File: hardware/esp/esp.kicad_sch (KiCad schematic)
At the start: 0 parts

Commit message: Updating PCB
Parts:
- added J1: USB_C_Receptacle_USB2.0_16P, Connector_USB:USB_C_Receptacle_HCTL_HC-TYPE-C-16P-01A, symbol Connector:USB_C_Receptacle_USB2.0_16P
- added J2: Conn_01x02, symbol Connector_Generic:Conn_01x02
- added L1: L, symbol Device:L
- added R1, R2: 22R, symbol Device:R
- added U1: BME280, Package_LGA:Bosch_LGA-8_2.5x2.5mm_P0.65mm_ClockwisePinNumbering, symbol Sensor:BME280
- added U2: VL53L0X, VL53L0X:SENSOR_VL53L0X, symbol VL53L0X:VL53L0X
- added U3: NRF24L01, Package_DFN_QFN:QFN-20-1EP_4x4mm_P0.5mm_EP2.5x2.5mm, symbol RF:NRF24L01
- added U4: ESP32-S3-WROOM-1, RF_Module:ESP32-S3-WROOM-1, symbol RF_Module:ESP32-S3-WROOM-1
- added U5: NT3H1101W0FHK, NT3H1101W0FHK:IC_NT3H1101W0FHK, symbol NT3H1101W0FHK:NT3H1101W0FHK
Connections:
- new net: U4.1 (GND), U4.40 (GND), U4.41 (GND)
- new net: L1.1, U5.8 (LB)
- new net: L1.2, U5.1 (LA)
- new net: J1.A6 (D+), J1.B6 (D+), R2.1
- new net: J1.A7 (D-), J1.B7 (D-), R1.1
- new net +5V: J1.A4 (VBUS), J1.A9 (VBUS), J1.B4 (VBUS), J1.B9 (VBUS)
- new net D+: R2.2, U4.14 (USB_D+)
- new net D-: R1.2, U4.13 (USB_D-)
- new net GND: J1.A1 (GND), J1.A12 (GND), J1.B1 (GND), J1.B12 (GND), J1.SH (SHIELD), U2.12 (GND), U2.3 (GND), U2.4 (GND), U2.6 (GND)
- new net UART_SRX: J2.2 (Pin_2)
- new net UART_STX: J2.1 (Pin_1)

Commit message: Updating schematics
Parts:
- removed U3: NRF24L01, Package_DFN_QFN:QFN-20-1EP_4x4mm_P0.5mm_EP2.5x2.5mm, symbol RF:NRF24L01
- added C1: 10nF, Capacitor_SMD:C_0603_1608Metric, symbol Device:C
- added C10, C11: C, symbol Device:C
- added C12: 100nF, symbol Device:C
- added C13: 4.7pF, symbol Device:C
- added C2: 33nF, Capacitor_SMD:C_0603_1608Metric, symbol Device:C
- added C3: 1nF, Capacitor_SMD:C_0603_1608Metric, symbol Device:C
- added C4: 2.2pF, Capacitor_SMD:C_0603_1608Metric, symbol Device:C
- added C5, C6: 22pF, Capacitor_SMD:C_0603_1608Metric, symbol Device:C
- added C7: 4.7pF, Capacitor_SMD:C_0603_1608Metric, symbol Device:C
- added C8: 1.5pF, Capacitor_SMD:C_0603_1608Metric, symbol Device:C
- added C9: 1pF, Capacitor_SMD:C_0603_1608Metric, symbol Device:C
- added L2: 8.2nH, Inductor_SMD:L_0603_1608Metric, symbol Device:L
- added L3, L4: 2.7nH, Inductor_SMD:L_0603_1608Metric, symbol Device:L
- added R1: 22K, Resistor_SMD:R_0603_1608Metric, symbol Device:R
- added R10, R11, R12: R, symbol Device:R
- added R13, R7, R8, R9: 1.5K, symbol Device:R
- added R4, R5: 5.1k, symbol Device:R
- added R6: 1M, Resistor_SMD:R_0603_1608Metric, symbol Device:R
- added U2: NRF24L01, Package_DFN_QFN:QFN-20-1EP_4x4mm_P0.5mm_EP2.5x2.5mm, symbol RF:NRF24L01
- added Y1: 16MHz, Crystal:Crystal_SMD_3225-4Pin_3.2x2.5mm, symbol Device:Crystal_GND24
- renumbered J2 to J3, R1 to R2, R2 to R3, U5 to U1, U4 to U3, U2 to U4, U1 to U5
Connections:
- net GND: now also U1.2 (VSS), U3.1 (GND), U3.40 (GND), U3.41 (GND), U4.2 (AVSSVCSEL), U5.1 (GND), U5.7 (GND), C1.1, C10.1, C11.2, C12.2, C13.2, C2.2, C3.1, C4.2, C5.1, C6.2, C7.2, C9.1, R1.1, R4.2, R5.2, U2.14 (VSS), U2.17 (VSS), U2.20 (VSS), U2.8 (VSS), Y1.2 (G), Y1.4 (G)
- net SDA: now reaches U3.12 (IO8)
- net SDA: now also U1.5 (SDA), U4.9 (SDA), U5.3 (SDI), R10.2, R7.2
- net SCL: now reaches U3.17 (IO9)
- net SCL: now also U1.3 (SCL), U4.10 (SCL), U5.4 (SCK), R11.1, R8.2
- net NFC_FD: now reaches U1.4 (FD)
- net +3V3: now reaches U1.6 (VCC)
- net +3V3: now also U4.1 (AVDDVCSEL), U4.11 (AVDD), U5.6 (VDDIO), U5.8 (VDD), C1.2, C10.2, C11.1, C12.1, C13.1, C3.2, R10.1, R11.2, R12.1, R13.1, R7.1, R8.1, R9.1, U2.15 (VDD), U2.18 (VDD), U2.7 (VDD)
- net XSHUT: now reaches U4.5 (~{XSHUT})
- net XSHUT: now also R9.2
- net DIST_GPIO1: now reaches U4.7 (GPIO1)
- net DIST_GPIO1: now also R13.2
- net at U5.2 (CSB): now also R12.2
- net at J1.A5 (CC1): now also R4.1
- net at J1.B5 (CC2): now also R5.1
- new net: C8.1, L3.2
- new net: C8.2, C9.2
- new net: L2.1, L3.1, U2.13 (ANT2)
- new net: C4.1, C7.1, L4.2, U2.11 (VDD_PA)
- new net: C5.2, R6.1, U2.10 (XC1), Y1.3
- new net: C6.1, R6.2, U2.9 (XC2), Y1.1
- new net: L2.2, L4.1, U2.12 (ANT1)
- new net: R1.2, U2.16 (IREF)
- new net: C2.1, U2.19 (DVDD)
- new net NRF_CE: U2.1 (CE)
- new net NRF_CSN: U2.2 (CSN)
- new net SPI_MISO: U2.5 (MISO)
- new net SPI_MOSI: U2.4 (MOSI)
- new net SPI_SCK: U2.3 (SCK)
- no-connect marks 0 -> 8
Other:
- note added: "ANT"
- note added: "NRF24l01"
- moved on the sheet: J3, L1, U1, U3, U4, U5

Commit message: Updating PCb and esp board schematics
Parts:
- added C10, C6: C, symbol Device:C
- added C12: 0.1µF, Capacitor_SMD:C_0805_2012Metric, symbol Device:C
- added D1, D2, D3, D4, D5, D6, D7: LED, symbol Device:LED
- added R1, R11, R12, R13, R14, R15, R2: R, symbol Device:R
- added R10: 10K, Resistor_SMD:R_0805_2012Metric, symbol Device:R
- added R9: 10k, Resistor_SMD:R_0805_2012Metric, symbol Device:R
- added SW1: RESET, Button_Switch_SMD:SW_SPST_SKQG_WithStem, symbol Switch:SW_Push
- added SW2: BOOT, Button_Switch_SMD:SW_SPST_SKQG_WithStem, symbol Switch:SW_Push
- C13: renamed from C10; footprint (none) -> Capacitor_SMD:C_0603_1608Metric
- C14: renamed from C12; footprint (none) -> Capacitor_SMD:C_0603_1608Metric
- C15: renamed from C11; footprint (none) -> Capacitor_SMD:C_0603_1608Metric
- C16: renamed from C13; footprint (none) -> Capacitor_SMD:C_0603_1608Metric
- R16: renamed from R7; footprint (none) -> Resistor_SMD:R_0805_2012Metric
- R17: renamed from R8; footprint (none) -> Resistor_SMD:R_0805_2012Metric
- R18: renamed from R9; footprint (none) -> Resistor_SMD:R_0805_2012Metric
- R19: renamed from R10; footprint (none) -> Resistor_SMD:R_0805_2012Metric
- R20: renamed from R13; footprint (none) -> Resistor_SMD:R_0805_2012Metric
- R21: renamed from R11; footprint (none) -> Resistor_SMD:R_0805_2012Metric
- R22: renamed from R12; footprint (none) -> Resistor_SMD:R_0805_2012Metric
- R4: renamed from R2; footprint (none) -> Resistor_SMD:R_0805_2012Metric
- R5: renamed from R3; footprint (none) -> Resistor_SMD:R_0805_2012Metric
- R6: renamed from R4; footprint (none) -> Resistor_SMD:R_0805_2012Metric
- R7: renamed from R5; footprint (none) -> Resistor_SMD:R_0805_2012Metric
- R8: renamed from R6; footprint Resistor_SMD:R_0603_1608Metric -> Resistor_SMD:R_0805_2012Metric
- renumbered C9 to C11, C3 to C2, C2 to C3, C5 to C4, C4 to C5, C6 to C7, C7 to C8, C8 to C9, J3 to J2, R1 to R3
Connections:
- net +3V3: now also U3.2 (3V3), C10.2, C6.2, R10.1, R9.2
- net GND: now also C10.1, C12.1, C6.1, D1.1 (K), D2.1 (K), D5.1 (K), D6.1 (K), D7.1 (K), SW1.2, SW2.2; no longer U2.20 (VSS)
- net C.SKULL: now reaches U3.15 (IO3)
- net C.SKULL: now also R14.1
- net BOOT: now reaches U3.27 (IO0)
- net BOOT: now also R10.2, SW2.1
- net EN: now reaches U3.3 (EN)
- net EN: now also C12.2, R9.1, SW1.1
- net O.SKULL: now reaches U3.38 (IO2)
- net O.SKULL: now also R13.1
- net NRFLED: now reaches U3.39 (IO1)
- net NRFLED: now also R2.1
- net NF.SKULL: now reaches U3.4 (IO4)
- net NF.SKULL: now also R15.1
- net NFCLED: now reaches U3.5 (IO5)
- net NFCLED: now also R1.1
- new net: D7.2 (A), R15.2
- new net: D2.2 (A), R2.2
- new net: D3.2 (A), R11.2
- new net: D5.2 (A), R13.2
- new net: D1.2 (A), R1.2
- new net: D4.2 (A), R12.2
- new net: D6.2 (A), R14.2
- no-connect marks 8 -> 10
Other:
- note added: "MCU"
- note added: "NFC chip"
- note added: "Skull opening detector"
- note added: "Temperature sensor"
- moved on the sheet: C1, C14, C16, C2, C4, J2, L1, R16, R17, R18, R20, U1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

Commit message: Updating schematics and PCB
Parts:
- removed C11: 1pF, Capacitor_SMD:C_0603_1608Metric, symbol Device:C
- removed C13, C15: C, Capacitor_SMD:C_0603_1608Metric, symbol Device:C
- removed C14: 100nF, Capacitor_SMD:C_0603_1608Metric, symbol Device:C
- removed C16, C8: 4.7pF, Capacitor_SMD:C_0603_1608Metric, symbol Device:C
- removed C5: 2.2pF, Capacitor_SMD:C_0603_1608Metric, symbol Device:C
- removed C7: 22pF, Capacitor_SMD:C_0603_1608Metric, symbol Device:C
- removed C9: 1.5pF, Capacitor_SMD:C_0603_1608Metric, symbol Device:C
- removed D2, D5, D6, D7: LED, symbol Device:LED
- removed L1: L, symbol Device:L
- removed L2: 8.2nH, Inductor_SMD:L_0603_1608Metric, symbol Device:L
- removed L3, L4: 2.7nH, Inductor_SMD:L_0603_1608Metric, symbol Device:L
- removed R1, R13, R14, R15, R2: R, symbol Device:R
- removed R16, R17, R18, R20: 1.5K, Resistor_SMD:R_0805_2012Metric, symbol Device:R
- removed R19, R21, R22: R, Resistor_SMD:R_0805_2012Metric, symbol Device:R
- removed R3: 22K, Resistor_SMD:R_0603_1608Metric, symbol Device:R
- removed R8: 1M, Resistor_SMD:R_0805_2012Metric, symbol Device:R
- removed U1: NT3H1101W0FHK, NT3H1101W0FHK:IC_NT3H1101W0FHK, symbol NT3H1101W0FHK:NT3H1101W0FHK
- removed U2: NRF24L01, Package_DFN_QFN:QFN-20-1EP_4x4mm_P0.5mm_EP2.5x2.5mm, symbol RF:NRF24L01
- removed U4: VL53L0X, VL53L0X:SENSOR_VL53L0X, symbol VL53L0X:VL53L0X
- removed U5: BME280, Package_LGA:Bosch_LGA-8_2.5x2.5mm_P0.65mm_ClockwisePinNumbering, symbol Sensor:BME280
- removed Y1: 16MHz, Crystal:Crystal_SMD_3225-4Pin_3.2x2.5mm, symbol Device:Crystal_GND24
- added J3: USB_C_Receptacle_USB2.0_16P, Connector_USB:USB_C_Receptacle_HCTL_HC-TYPE-C-16P-01A, symbol Connector:USB_C_Receptacle_USB2.0_16P
- added J4: Conn_01x01_Pin, Connector_PinHeader_1.00mm:PinHeader_1x01_P1.00mm_Vertical, symbol Connector:Conn_01x01_Pin
- added Q1: MMBT3906, Package_TO_SOT_SMD:SOT-23, symbol Transistor_BJT:MMBT3906
- added R23, R24: 22R, Resistor_SMD:R_0805_2012Metric, symbol Device:R
- added R25, R26: 5.1k, Resistor_SMD:R_0805_2012Metric, symbol Device:R
- added R5: R, Resistor_SMD:R_0805_2012Metric, symbol Device:R
- added U1: AMS1117-3.3, Package_TO_SOT_SMD:SOT-223-3_TabPin2, symbol Regulator_Linear:AMS1117-3.3
- added U6: CP2102N-Axx-xQFN20, Package_DFN_QFN:SiliconLabs_QFN-20-1EP_3x3mm_P0.5mm_EP1.8x1.8mm, symbol Interface_USB:CP2102N-Axx-xQFN20
- C1: value 10nF -> 10uF; footprint Capacitor_SMD:C_0603_1608Metric -> Capacitor_SMD:C_0805_2012Metric
- C2: value 1nF -> 0.1uF; footprint Capacitor_SMD:C_0603_1608Metric -> Capacitor_SMD:C_0805_2012Metric
- C3: value 33nF -> 10uF; footprint Capacitor_SMD:C_0603_1608Metric -> Capacitor_SMD:C_0805_2012Metric
- C4: value 22pF -> 0.1uF; footprint Capacitor_SMD:C_0603_1608Metric -> Capacitor_SMD:C_0805_2012Metric
- C5: renamed from C6; footprint (none) -> Capacitor_SMD:C_0805_2012Metric
- C7: renamed from C10; footprint (none) -> Capacitor_SMD:C_0805_2012Metric
- D1: footprint (none) -> LED_SMD:LED_0603_1608Metric
- D2: renamed from D3; footprint (none) -> LED_SMD:LED_0603_1608Metric
- D3: renamed from D4; footprint (none) -> LED_SMD:LED_0603_1608Metric
- J2: footprint (none) -> Connector_PinHeader_2.54mm:PinHeader_1x02_P2.54mm_Vertical
- R8: renamed from R11; footprint (none) -> Resistor_SMD:R_0805_2012Metric
- R9: renamed from R12; footprint (none) -> Resistor_SMD:R_0805_2012Metric
- renumbered C12 to C6, R4 to R1, R5 to R2, R6 to R3, R7 to R4, R9 to R6, R10 to R7, U3 to U2
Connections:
- net +3V3: now also C3.1, C4.1, R5.2, U1.2 (VO); no longer C1.2, C2.2
- net +5V: now also C1.1, C2.1, J3.A4 (VBUS), J3.A9 (VBUS), J3.B4 (VBUS), J3.B9 (VBUS), J4.1 (Pin_1), U1.3 (VI)
- net D+: now also R24.2
- net D-: now also R23.2
- net GND: now also C1.2, C2.2, C4.2, J3.A1 (GND), J3.A12 (GND), J3.B1 (GND), J3.B12 (GND), J3.SH (SHIELD), R25.2, R26.2, U1.1 (GND); no longer C1.1, C2.1, C4.1
- net at D1.2 (A): now also R5.1
- net NFCLED: no longer names the net of U2.5 (IO5)
- new net: J3.A5 (CC1), R25.1
- new net: J3.A6 (D+), J3.B6 (D+), R24.1
- new net: J3.B5 (CC2), R26.1
- new net: J3.A7 (D-), J3.B7 (D-), R23.1
- new net: U6.12 (GND), U6.21 (GND), U6.3 (GND)
- no-connect marks 10 -> 9
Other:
- note removed: "ANT"
- note removed: "NFC chip"
- note removed: "NRF24l01"
- note removed: "Skull opening detector"
- note removed: "Temperature sensor"
- moved on the sheet: C6, D2, D3, J2, R6, R7, R8, R9, SW1, SW2

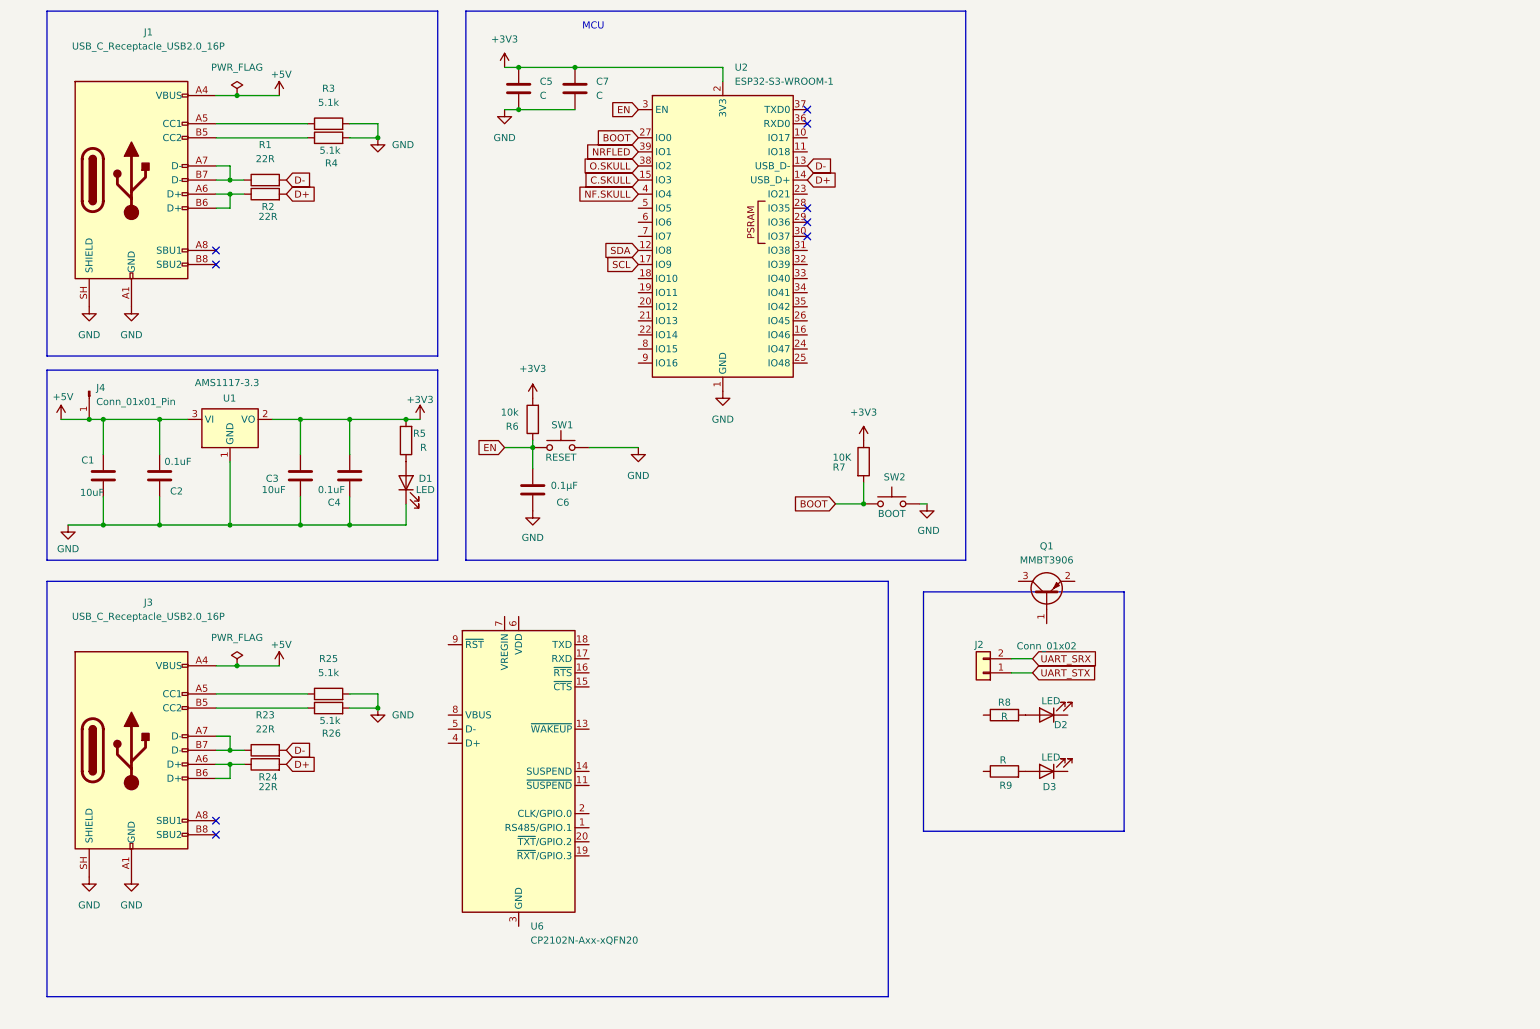
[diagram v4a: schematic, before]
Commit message: Updating pins, working on schematic and placing components on PCB
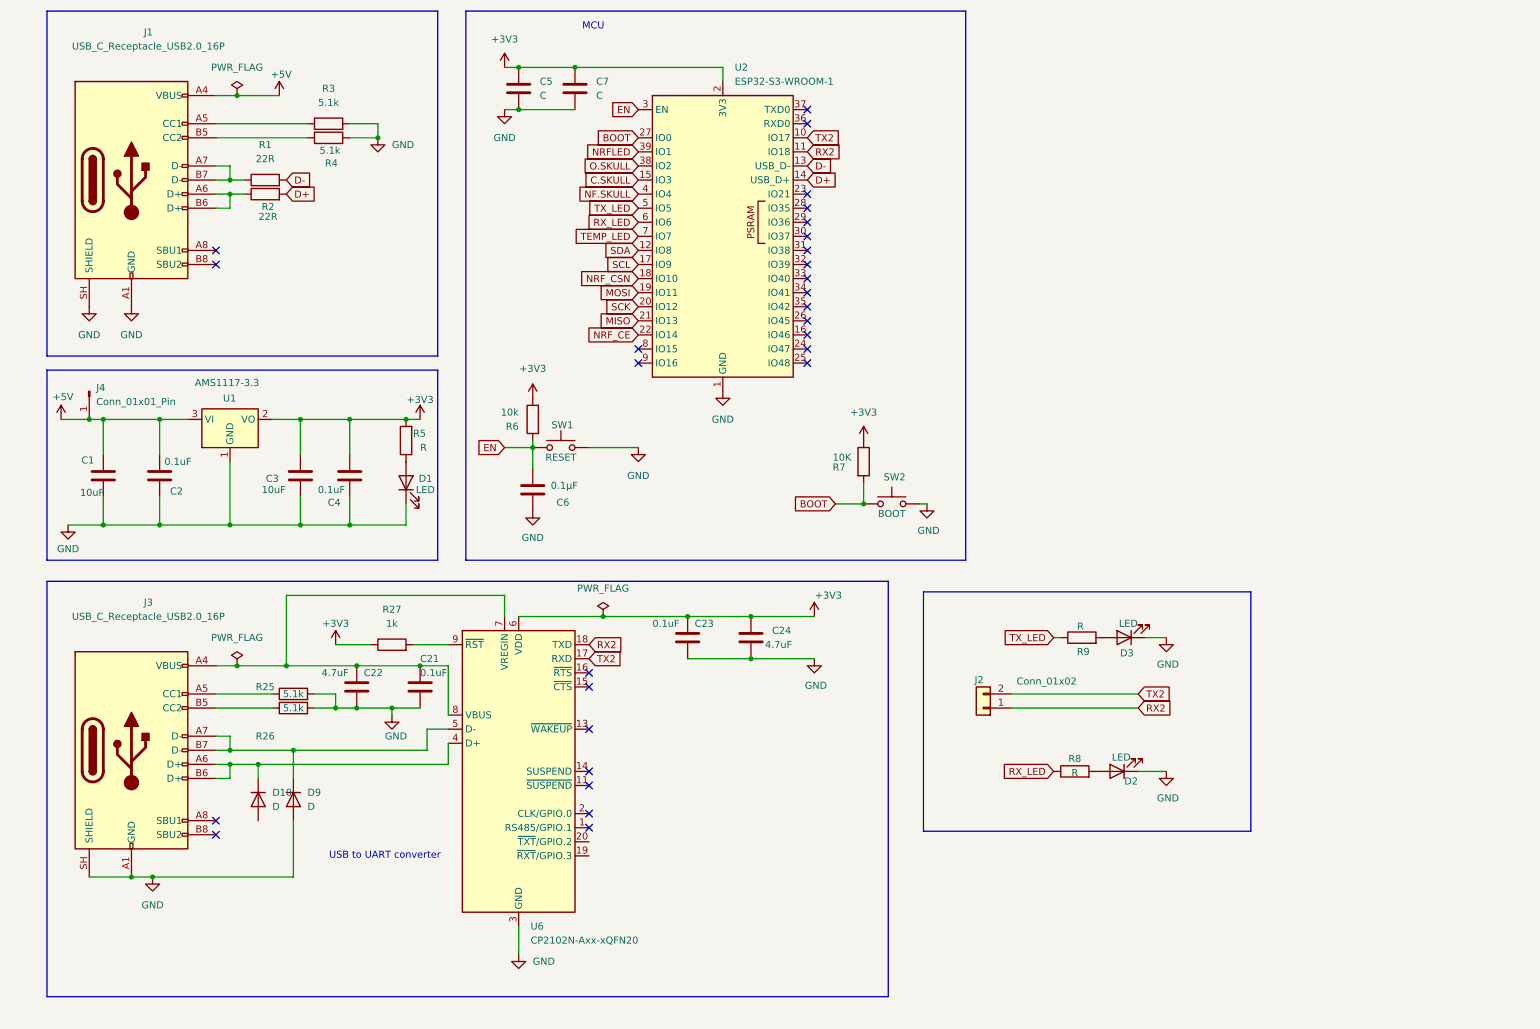
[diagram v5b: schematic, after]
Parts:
- removed Q1: MMBT3906, Package_TO_SOT_SMD:SOT-23, symbol Transistor_BJT:MMBT3906
- removed R23, R24: 22R, Resistor_SMD:R_0805_2012Metric, symbol Device:R
- added C21, C23: 0.1uF, Capacitor_SMD:C_0805_2012Metric, symbol Device:C
- added C22, C24: 4.7uF, Capacitor_SMD:C_0805_2012Metric, symbol Device:C
- added D10, D9: D, symbol Device:D
- added R27: 1k, Resistor_SMD:R_0805_2012Metric, symbol Device:R
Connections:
- net UART_SRX is gone; now on net TX2: J2.2 (Pin_2)
- net UART_STX is gone; now on net RX2: J2.1 (Pin_1)
- net +3V3: now also U6.6 (VDD), C23.1, C24.1, R27.1
- net +5V: no longer J3.A4 (VBUS), J3.A9 (VBUS), J3.B4 (VBUS), J3.B9 (VBUS)
- net GND: now also D2.1 (K), D3.1 (K), U6.12 (GND), U6.21 (GND), U6.3 (GND), C21.2, C22.2, C23.2, C24.2, D9.2 (A)
- net TX2: now reaches U2.10 (IO17)
- net TX2: now also U6.17 (RXD)
- net RX2: now reaches U2.11 (IO18)
- net RX2: now also U6.18 (TXD)
- net NRF_CSN: now reaches U2.18 (IO10)
- net MOSI: now reaches U2.19 (IO11)
- net SCK: now reaches U2.20 (IO12)
- net MISO: now reaches U2.21 (IO13)
- net NRF_CE: now reaches U2.22 (IO14)
- net TX_LED: now reaches U2.5 (IO5)
- net TX_LED: now also R9.1
- net RX_LED: now reaches U2.6 (IO6)
- net RX_LED: now also R8.1
- net TEMP_LED: now reaches U2.7 (IO7)
- net at J3.A6 (D+), J3.B6 (D+): now also U6.4 (D+), D10.1 (K)
- net at J3.A7 (D-), J3.B7 (D-): now also U6.5 (D-), D9.1 (K)
- net at U6.7 (VREGIN): now also J3.A4 (VBUS), J3.A9 (VBUS), J3.B4 (VBUS), J3.B9 (VBUS), U6.8 (VBUS), C21.1, C22.1
- net at U6.9 (~{RST}): now also R27.2
- no-connect marks 9 -> 28
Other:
- note added: "USB to UART converter"
- title: (none) -> E.L.B.E.R.R Fanmade ESP PCB
- moved on the sheet: D2, D3, J2, R25, R26, R8, R9
